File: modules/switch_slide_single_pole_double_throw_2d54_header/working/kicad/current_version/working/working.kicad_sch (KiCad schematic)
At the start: 1 part, among them J1 swsi1h

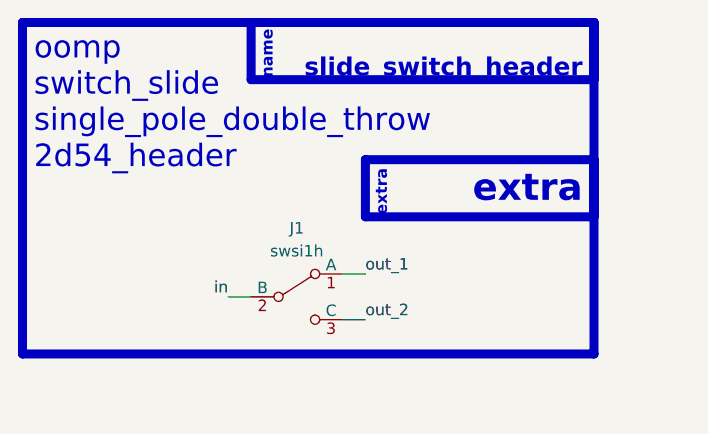
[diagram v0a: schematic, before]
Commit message: fixed formatting to be more consistent
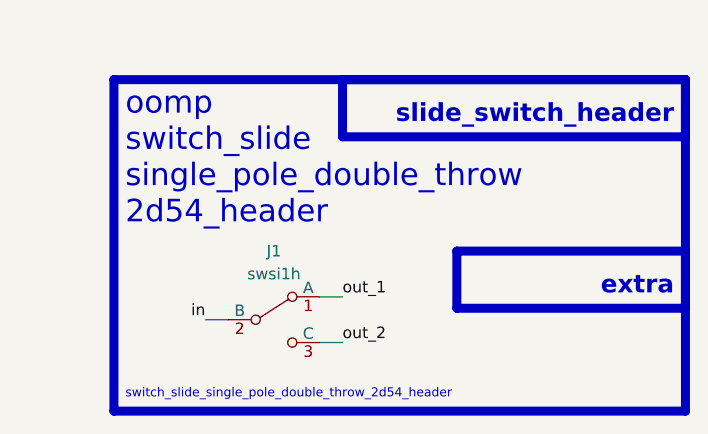
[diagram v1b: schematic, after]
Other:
- note added: "switch_slide_single_pole_double_throw_2d54_header"
- note removed: "name"
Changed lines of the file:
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@@
 (kicad_sch (version 20230121) (generator eeschema)
   (paper "A4")
-  (wire (pts (xy 142.24 83.82) (xy 144.78 83.82))
+  (wire (pts (xy 139.7 91.44) (xy 142.24 91.44))
     (stroke (width 0) (type default))
   )
-  (wire (pts (xy 129.54 86.36) (xy 132.08 86.36))
+  (wire (pts (xy 127 88.9) (xy 129.54 88.9))
     (stroke (width 0) (type default))
   )
-  (wire (pts (xy 142.24 88.9) (xy 144.78 88.9))
+  (wire (pts (xy 139.7 86.36) (xy 142.24 86.36))
     (stroke (width 0) (type default))
   )
-  (rectangle (start 106.68 55.88) (end 170.18 92.71)
+  (rectangle (start 142.24 62.23) (end 180.34 68.58)
     (stroke (width 1) (type default))
     (fill (type none))
@@
     (fill (type none))
   )
-  (rectangle (start 132.08 55.88) (end 170.18 62.23)
-    (stroke (width 1) (type default))
-    (fill (type color) (color 0 0 0 0))
-  )
-  (rectangle (start 144.78 71.12) (end 170.18 77.47)
+  (rectangle (start 154.94 81.28) (end 180.34 87.63)
     (stroke (width 1) (type default))
     (fill (type none))
   )
-  (text "slide_switch_header" (at 168.91 62.23 0)
-    (effects (font (size 2 2) (thickness 0.8) bold (color 255 255 255 1)) (justify right bottom))
+  (rectangle (start 116.84 62.23) (end 180.34 99.06)
+    (stroke (width 1) (type default))
+    (fill (type none))
   )
-  (text "name" (at 134.62 62.23 90)
-    (effects (font (size 1.27 1.27) (thickness 0.254) bold (color 255 255 255 1)) (justify left bottom))
+  (text "switch_slide_single_pole_double_throw_2d54_header" (at 118.11 97.79 0)
+    (effects (font (size 1 1)) (justify left bottom))
   )
-  (text "extra" (at 168.91 76.2 0)
-    (effects (font (size 3 3) (thickness 0.8) bold) (justify right bottom))
+  (text "extra" (at 179.07 86.36 0)
+    (effects (font (size 2 2) (thickness 0.8) bold) (justify right bottom))
   )
-  (text "oomp\nswitch_slide\nsingle_pole_double_throw\n2d54_header\n"
-    (at 107.95 72.39 0)
+  (text "oomp\nswitch_slide\nsingle_pole_double_throw\n2d54_header\n\n"
+    (at 118.11 82.55 0)
     (effects (font (size 2.5 2.5)) (justify left bottom))
   )
-  (text "extra" (at 147.32 77.47 90)
-    (effects (font (size 1.27 1.27) (thickness 0.254) bold) (justify left bottom))
+  (text "slide_switch_header" (at 179.07 67.31 0)
+    (effects (font (size 2 2) (thickness 0.8) bold) (justify right bottom))
   )
-  (label "out_2" (at 144.78 88.9 0) (fields_autoplaced)
+  (label "in" (at 127 88.9 180) (fields_autoplaced)
+    (effects (font (size 1.27 1.27)) (justify right bottom))
+  )
+  (label "out_1" (at 142.24 86.36 0) (fields_autoplaced)
     (effects (font (size 1.27 1.27)) (justify left bottom))
   )
-  (label "in" (at 129.54 86.36 180) (fields_autoplaced)
-    (effects (font (size 1.27 1.27)) (justify right bottom))
-  )
-  (label "out_1" (at 144.78 83.82 0) (fields_autoplaced)
+  (label "out_2" (at 142.24 91.44 0) (fields_autoplaced)
     (effects (font (size 1.27 1.27)) (justify left bottom))
   )
-  (symbol (lib_id "oomlout_oomp_part_symbols:swsi1h_electronic_switch_slide_2d54_header_single_pole_double_throw") (at 137.16 86.36 0) (unit 1)
-    (in_bom yes) (on_board yes) (dnp no) (fields_autoplaced)
-    (property "Reference" "J1" (at 137.16 78.74 0)
+  (symbol (lib_id "oomlout_oomp_part_symbols:swsi1h_electronic_switch_slide_2d54_header_single_pole_double_throw") (at 134.62 88.9 0) (unit 1)
+    (in_bom yes) (on_board yes) (dnp no)
+    (property "Reference" "J1" (at 134.62 81.28 0)
       (effects (font (size 1.27 1.27)))
     )
-    (property "Value" "swsi1h" (at 137.16 81.28 0)
+    (property "Value" "swsi1h" (at 134.62 83.82 0)
       (effects (font (size 1.27 1.27)))
     )
-    (property "Footprint" "oomlout_oomp_part_footprints:swsi1h_electronic_switch_slide_2d54_header_single_pole_double_throw" (at 137.16 86.36 0)
+    (property "Footprint" "oomlout_oomp_part_footprints:swsi1h_electronic_switch_slide_2d54_header_single_pole_double_throw" (at 134.62 88.9 0)
       (effects (font (size 1.27 1.27)) hide)
     )
-    (property "Datasheet" "https://github.com/oomlout/oomlout_oomp_v3/parts/electronic_switch_slide_2d54_header_single_pole_double_throw/datasheet.pdf" (at 137.16 86.36 0)
+    (property "Datasheet" "https://github.com/oomlout/oomlout_oomp_v3/parts/electronic_switch_slide_2d54_header_single_pole_double_throw/datasheet.pdf" (at 134.62 88.9 0)
       (effects (font (size 1.27 1.27)) hide)
     )

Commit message: a few fix ups
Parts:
- removed J1: swsi1h, oomlout_oomp_part_footprints:swsi1h_electronic_switch_slide_2d54_header_single_pole_double_throw, symbol oomlout_oomp_part_symbols:swsi1h_electronic_switch_slide_2d54_header_single_pol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
- added SW1: swsi1h, oomlout_oomp_part_footprints:swsi1h_electronic_switch_slide_2d54_header_single_pole_double_throw, symbol oomlout_oomp_part_symbols:swsi1h_electronic_switch_slide_2d54_header_single_pol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
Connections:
- new net slide_switch_in: SW1.2 (B)
- new net slide_switch_out_1: SW1.1 (A)
- new net slide_switch_out_2: SW1.3 (C)
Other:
- note added: "switch_slide_single_pole_double_throw_2_8_mm_x_8_mm_x_1_4"
- note removed: "switch_slide_single_pole_double_throw_2d54_header"
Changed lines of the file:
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@@
 (kicad_sch (version 20230121) (generator eeschema)
   (paper "A4")
-  (wire (pts (xy 139.7 91.44) (xy 142.24 91.44))
+  (wire (pts (xy 137.16 111.76) (xy 139.7 111.76))
     (stroke (width 0) (type default))
   )
-  (wire (pts (xy 127 88.9) (xy 129.54 88.9))
+  (wire (pts (xy 137.16 106.68) (xy 139.7 106.68))
     (stroke (width 0) (type default))
   )
-  (wire (pts (xy 139.7 86.36) (xy 142.24 86.36))
+  (wire (pts (xy 124.46 109.22) (xy 127 109.22))
     (stroke (width 0) (type default))
   )
-  (rectangle (start 142.24 62.23) (end 180.34 68.58)
+  (rectangle (start 102.87 71.12) (end 166.37 120.65)
     (stroke (width 1) (type default))
     (fill (type none))
@@
     (fill (type none))
   )
-  (rectangle (start 154.94 81.28) (end 180.34 87.63)
+  (rectangle (start 128.27 90.17) (end 166.37 96.52)
     (stroke (width 1) (type default))
     (fill (type none))
   )
-  (rectangle (start 116.84 62.23) (end 180.34 99.06)
+  (rectangle (start 147.32 234.95) (end 147.32 234.95)
+    (stroke (width 0) (type default))
+    (fill (type none))
+  )
+  (rectangle (start 128.27 71.12) (end 166.37 77.47)
     (stroke (width 1) (type default))
     (fill (type none))
   )
-  (text "switch_slide_single_pole_double_throw_2d54_header" (at 118.11 97.79 0)
+  (text "oomp\nswitch_slide\nsingle_pole_double_throw\n2d54_header\n\n"
+    (at 104.14 91.44 0)
+    (effects (font (size 2.5 2.5)) (justify left bottom))
+  )
+  (text "extra" (at 165.1 95.25 0)
+    (effects (font (size 2 2) (thickness 0.8) bold) (justify right bottom))
+  )
+  (text "slide_switch_header" (at 165.1 76.2 0)
+    (effects (font (size 2 2) (thickness 0.8) bold) (justify right bottom))
+  )
+  (text "switch_slide_single_pole_double_throw_2_8_mm_x_8_mm_x_1_4"
+    (at 104.14 119.38 0)
     (effects (font (size 1 1)) (justify left bottom))
   )
-  (text "extra" (at 179.07 86.36 0)
-    (effects (font (size 2 2) (thickness 0.8) bold) (justify right bottom))
-  )
-  (text "oomp\nswitch_slide\nsingle_pole_double_throw\n2d54_header\n\n"
-    (at 118.11 82.55 0)
-    (effects (font (size 2.5 2.5)) (justify left bottom))
-  )
-  (text "slide_switch_header" (at 179.07 67.31 0)
-    (effects (font (size 2 2) (thickness 0.8) bold) (justify right bottom))
-  )
-  (label "in" (at 127 88.9 180) (fields_autoplaced)
+  (label "slide_switch_in" (at 124.46 109.22 180) (fields_autoplaced)
     (effects (font (size 1.27 1.27)) (justify right bottom))
   )
-  (label "out_1" (at 142.24 86.36 0) (fields_autoplaced)
+  (label "slide_switch_out_2" (at 139.7 111.76 0) (fields_autoplaced)
     (effects (font (size 1.27 1.27)) (justify left bottom))
   )
-  (label "out_2" (at 142.24 91.44 0) (fields_autoplaced)
+  (label "slide_switch_out_1" (at 139.7 106.68 0) (fields_autoplaced)
     (effects (font (size 1.27 1.27)) (justify left bottom))
   )
-  (symbol (lib_id "oomlout_oomp_part_symbols:swsi1h_electronic_switch_slide_2d54_header_single_pole_double_throw") (at 134.62 88.9 0) (unit 1)
-    (in_bom yes) (on_board yes) (dnp no)
-    (property "Reference" "J1" (at 134.62 81.28 0)
+  (symbol (lib_id "oomlout_oomp_part_symbols:swsi1h_electronic_switch_slide_2d54_header_single_pole_double_throw") (at 132.08 109.22 0) (unit 1)
+    (in_bom yes) (on_board yes) (dnp no) (fields_autoplaced)
+    (property "Reference" "SW1" (at 132.08 101.6 0)
       (effects (font (size 1.27 1.27)))
     )
-    (property "Value" "swsi1h" (at 134.62 83.82 0)
+    (property "Value" "swsi1h" (at 132.08 104.14 0)
       (effects (font (size 1.27 1.27)))
     )
-    (property "Footprint" "oomlout_oomp_part_footprints:swsi1h_electronic_switch_slide_2d54_header_single_pole_double_throw" (at 134.62 88.9 0)
+    (property "Footprint" "oomlout_oomp_part_footprints:swsi1h_electronic_switch_slide_2d54_header_single_pole_double_throw" (at 132.08 109.22 0)
       (effects (font (size 1.27 1.27)) hide)
     )
-    (property "Datasheet" "https://github.com/oomlout/oomlout_oomp_v3/parts/electronic_switch_slide_2d54_header_single_pole_double_throw/datasheet.pdf" (at 134.62 88.9 0)
+    (property "Datasheet" "https://github.com/oomlout/oomlout_oomp_v3/parts/electronic_switch_slide_2d54_header_single_pole_double_throw/datasheet.pdf" (at 132.08 109.22 0)
       (effects (font (size 1.27 1.27)) hide)
     )
@@
       (project "working"
         (path "/c9993764-076f-44f6-bf4c-6b69ce17c9e4"
-          (reference "J1") (unit 1)
+          (reference "SW1") (unit 1)
         )
       )

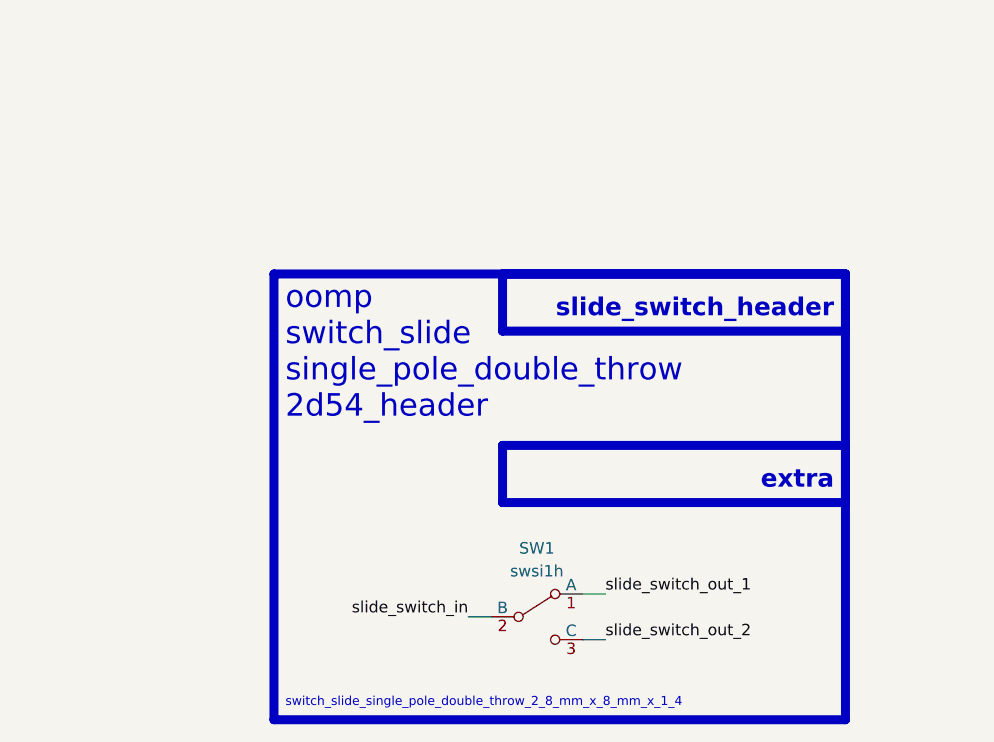
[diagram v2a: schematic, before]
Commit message: schematic formatting
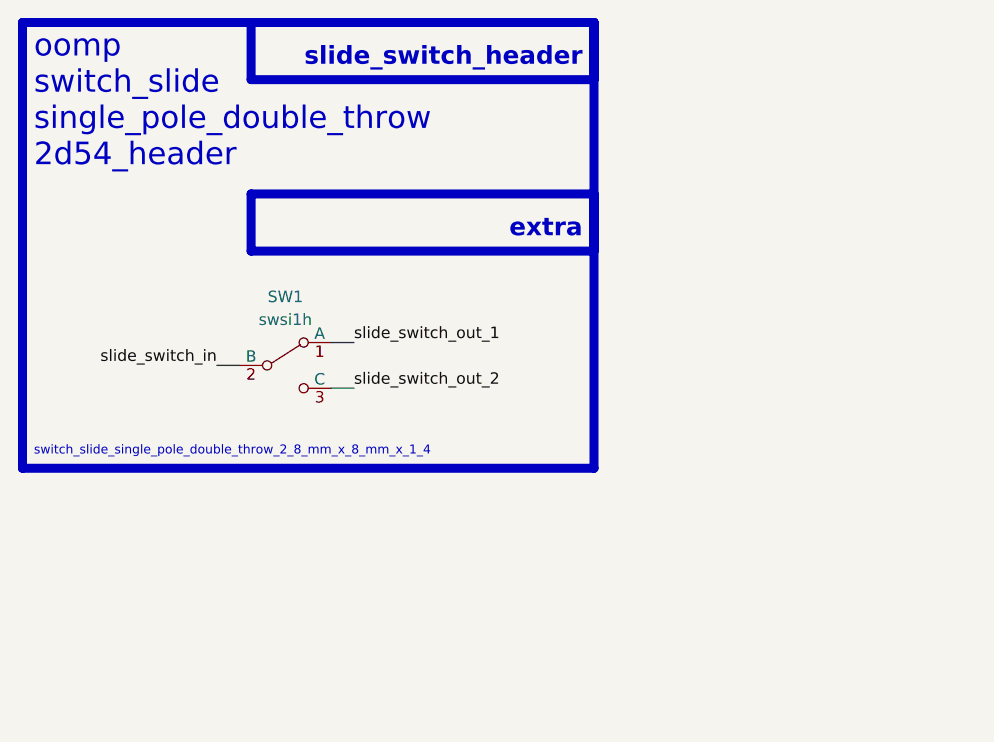
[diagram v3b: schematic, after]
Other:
- moved on the sheet: SW1
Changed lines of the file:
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@@
 (kicad_sch (version 20230121) (generator eeschema)
-  (paper "A4")
-  (wire (pts (xy 137.16 111.76) (xy 139.7 111.76))
+  (paper "A5")
+  (wire (pts (xy 109.22 83.82) (xy 111.76 83.82))
     (stroke (width 0) (type default))
   )
-  (wire (pts (xy 137.16 106.68) (xy 139.7 106.68))
+  (wire (pts (xy 109.22 78.74) (xy 111.76 78.74))
     (stroke (width 0) (type default))
   )
-  (wire (pts (xy 124.46 109.22) (xy 127 109.22))
+  (wire (pts (xy 96.52 81.28) (xy 99.06 81.28))
     (stroke (width 0) (type default))
   )
-  (rectangle (start 102.87 71.12) (end 166.37 120.65)
+  (rectangle (start 74.93 43.18) (end 138.43 92.71)
     (stroke (width 1) (type default))
     (fill (type none))
   )
-  (rectangle (start 151.13 219.71) (end 151.13 219.71)
+  (rectangle (start 123.19 191.77) (end 123.19 191.77)
     (stroke (width 0) (type default))
     (fill (type none))
   )
-  (rectangle (start 128.27 90.17) (end 166.37 96.52)
+  (rectangle (start 100.33 62.23) (end 138.43 68.58)
     (stroke (width 1) (type default))
     (fill (type none))
   )
-  (rectangle (start 147.32 234.95) (end 147.32 234.95)
+  (rectangle (start 119.38 207.01) (end 119.38 207.01)
     (stroke (width 0) (type default))
     (fill (type none))
   )
-  (rectangle (start 128.27 71.12) (end 166.37 77.47)
+  (rectangle (start 100.33 43.18) (end 138.43 49.53)
     (stroke (width 1) (type default))
     (fill (type none))
   )
   (text "oomp\nswitch_slide\nsingle_pole_double_throw\n2d54_header\n\n"
-    (at 104.14 91.44 0)
+    (at 76.2 63.5 0)
     (effects (font (size 2.5 2.5)) (justify left bottom))
   )
-  (text "extra" (at 165.1 95.25 0)
+  (text "extra" (at 137.16 67.31 0)
     (effects (font (size 2 2) (thickness 0.8) bold) (justify right bottom))
   )
-  (text "slide_switch_header" (at 165.1 76.2 0)
+  (text "slide_switch_header" (at 137.16 48.26 0)
     (effects (font (size 2 2) (thickness 0.8) bold) (justify right bottom))
   )
   (text "switch_slide_single_pole_double_throw_2_8_mm_x_8_mm_x_1_4"
-    (at 104.14 119.38 0)
+    (at 76.2 91.44 0)
     (effects (font (size 1 1)) (justify left bottom))
   )
-  (label "slide_switch_in" (at 124.46 109.22 180) (fields_autoplaced)
+  (label "slide_switch_in" (at 96.52 81.28 180) (fields_autoplaced)
     (effects (font (size 1.27 1.27)) (justify right bottom))
   )
-  (label "slide_switch_out_2" (at 139.7 111.76 0) (fields_autoplaced)
+  (label "slide_switch_out_2" (at 111.76 83.82 0) (fields_autoplaced)
     (effects (font (size 1.27 1.27)) (justify left bottom))
   )
-  (label "slide_switch_out_1" (at 139.7 106.68 0) (fields_autoplaced)
+  (label "slide_switch_out_1" (at 111.76 78.74 0) (fields_autoplaced)
     (effects (font (size 1.27 1.27)) (justify left bottom))
   )
-  (symbol (lib_id "oomlout_oomp_part_symbols:swsi1h_electronic_switch_slide_2d54_header_single_pole_double_throw") (at 132.08 109.22 0) (unit 1)
+  (symbol (lib_id "oomlout_oomp_part_symbols:swsi1h_electronic_switch_slide_2d54_header_single_pole_double_throw") (at 104.14 81.28 0) (unit 1)
     (in_bom yes) (on_board yes) (dnp no) (fields_autoplaced)
-    (property "Reference" "SW1" (at 132.08 101.6 0)
+    (property "Reference" "SW1" (at 104.14 73.66 0)
       (effects (font (size 1.27 1.27)))
     )
-    (property "Value" "swsi1h" (at 132.08 104.14 0)
+    (property "Value" "swsi1h" (at 104.14 76.2 0)
       (effects (font (size 1.27 1.27)))
     )
-    (property "Footprint" "oomlout_oomp_part_footprints:swsi1h_electronic_switch_slide_2d54_header_single_pole_double_throw" (at 132.08 109.22 0)
+    (property "Footprint" "oomlout_oomp_part_footprints:swsi1h_electronic_switch_slide_2d54_header_single_pole_double_throw" (at 104.14 81.28 0)
       (effects (font (size 1.27 1.27)) hide)
     )
-    (property "Datasheet" "https://github.com/oomlout/oomlout_oomp_v3/parts/electronic_switch_slide_2d54_header_single_pole_double_throw/datasheet.pdf" (at 132.08 109.22 0)
+    (property "Datasheet" "https://github.com/oomlout/oomlout_oomp_v3/parts/electronic_switch_slide_2d54_header_single_pole_double_throw/datasheet.pdf" (at 104.14 81.28 0)
       (effects (font (size 1.27 1.27)) hide)
     )
